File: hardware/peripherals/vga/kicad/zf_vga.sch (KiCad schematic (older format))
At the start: 35 parts

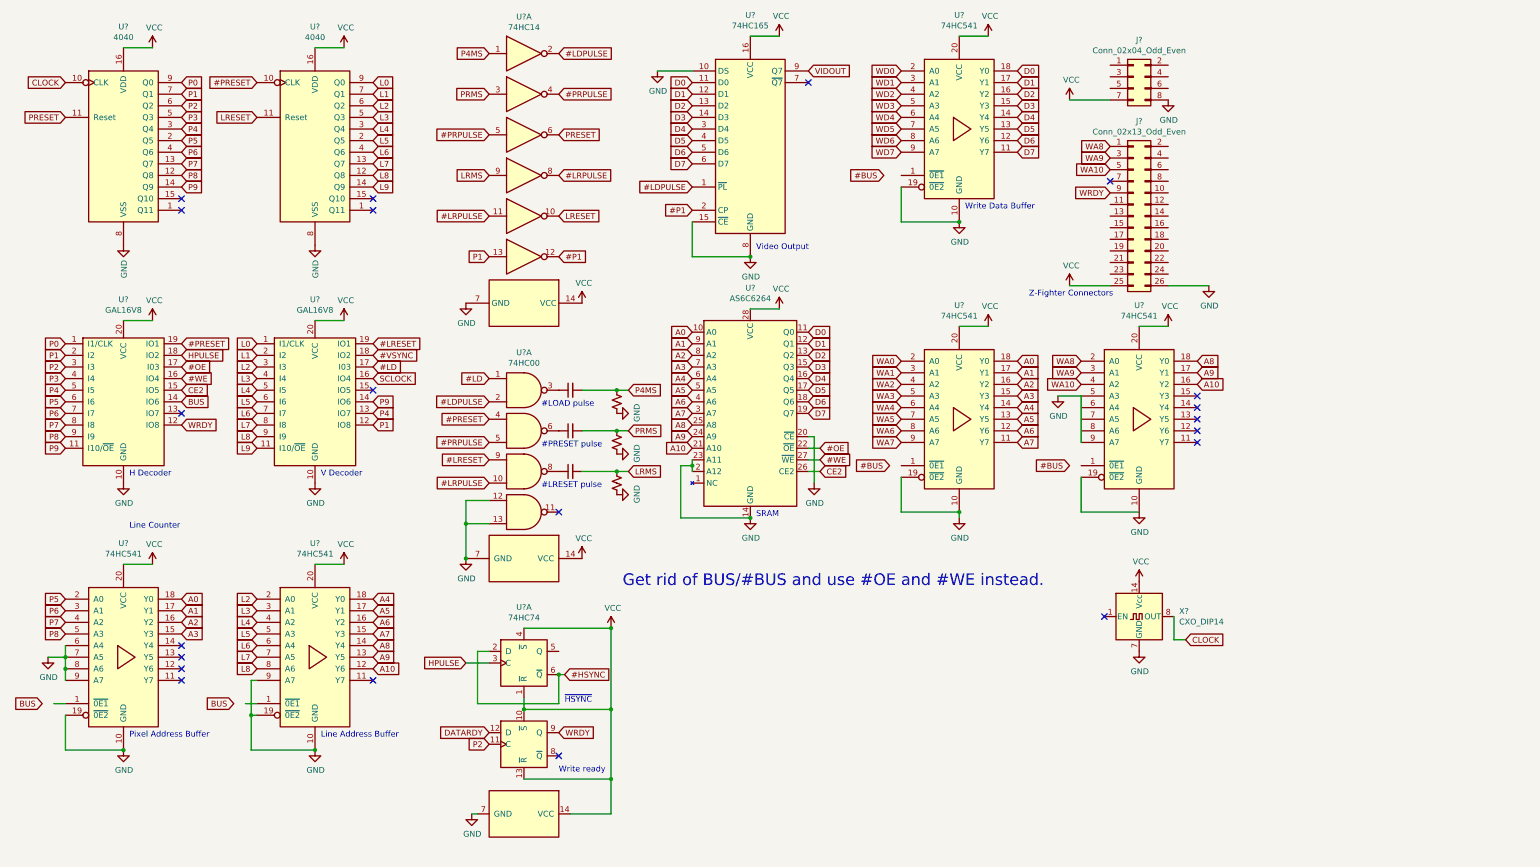
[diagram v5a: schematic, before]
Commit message: Changed /hsync to set/reset on flip flop, changed bus to /we and /oe
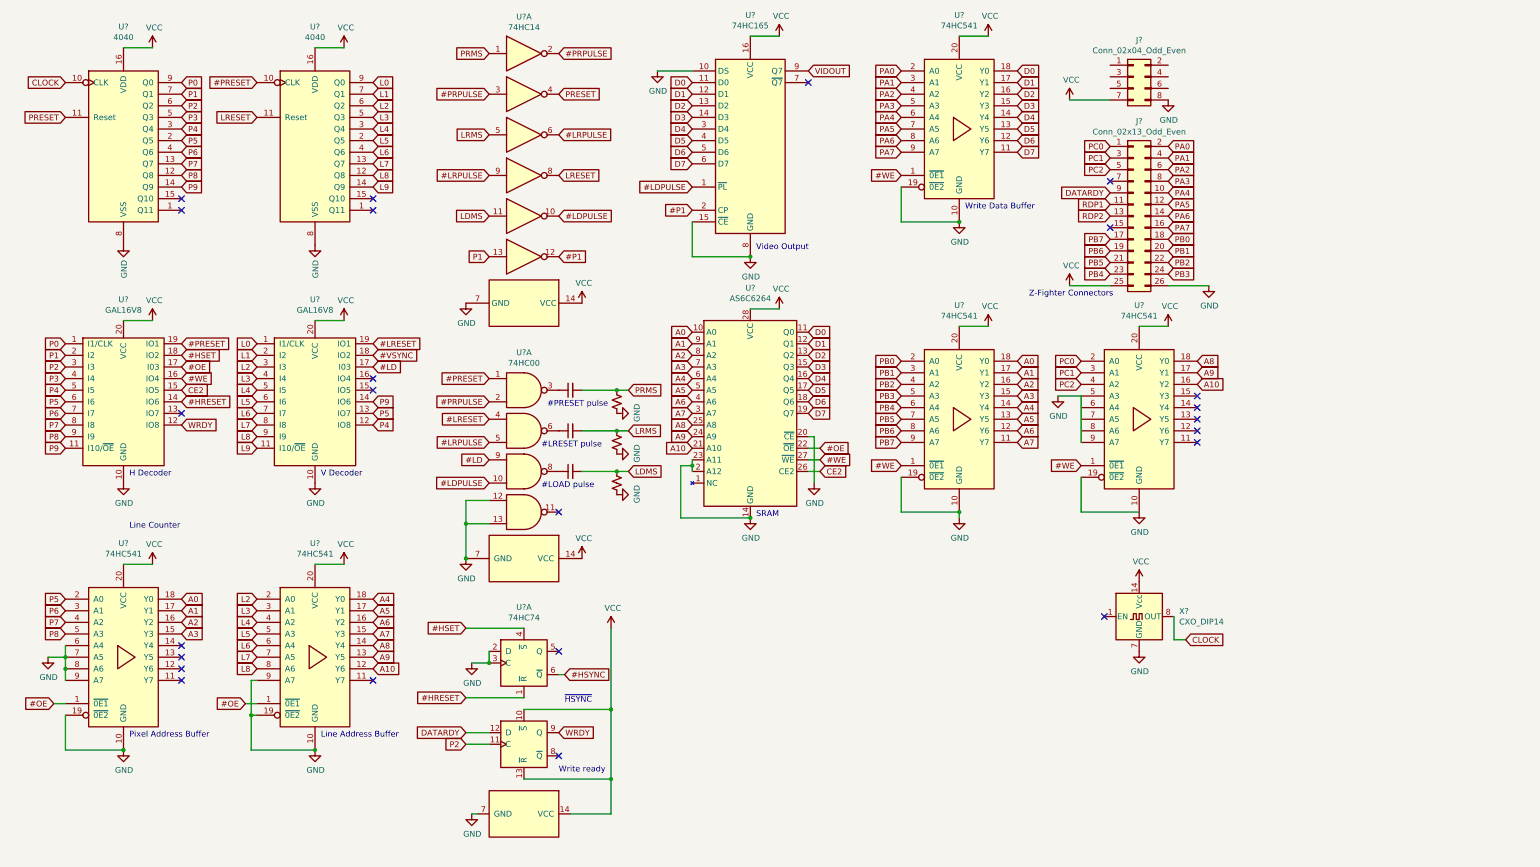
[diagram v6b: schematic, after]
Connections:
- net WA0 is gone; now on net PB0: U?.2 (A0)
- net WA1 is gone; now on net PB1: U?.3 (A1)
- net WA2 is gone; now on net PB2: U?.4 (A2)
- net WA3 is gone; now on net PB3: U?.5 (A3)
- net WA4 is gone; now on net PB4: U?.6 (A4)
- net WA5 is gone; now on net PB5: U?.7 (A5)
- net WA6 is gone; now on net PB6: U?.8 (A6)
- net WA7 is gone; now on net PB7: U?.9 (A7)
- net WD0 is gone; now on net PA0: U?.2 (A0)
- net WD1 is gone; now on net PA1: U?.3 (A1)
- net WD2 is gone; now on net PA2: U?.4 (A2)
- net WD3 is gone; now on net PA3: U?.5 (A3)
- net WD4 is gone; now on net PA4: U?.6 (A4)
- net WD5 is gone; now on net PA5: U?.7 (A5)
- net WD6 is gone; now on net PA6: U?.8 (A6)
- net WD7 is gone; now on net PA7: U?.9 (A7)
- net #HSYNC: no longer U?.2 (D)
- net #LD: now also U?.9; no longer U?.1
- net #LDPULSE: now also U?.10, U?.10; no longer U?.2, U?.2
- net #LRESET: now also U?.4; no longer U?.9
- net #LRPULSE: now also U?.5, U?.6, U?.9; no longer U?.10, U?.11, U?.8
- net #OE: now also U?.1 (~0E1), U?.1 (~0E1)
- net #PRESET: now also U?.1; no longer U?.4
- net #PRPULSE: now also U?.2, U?.2, U?.3; no longer U?.4, U?.5, U?.5
- net #WE: now also U?.1 (~0E1), U?.1 (~0E1), U?.1 (~0E1)
- net DATARDY: now also J?.9 (Pin_9)
- net GND: now also U?.2 (D), U?.3 (C)
- net LRESET: now also U?.8; no longer U?.10
- net LRMS: now also U?.5; no longer U?.9
- net P1: no longer U?.12 (IO8)
- net P4: now also U?.12 (IO8); no longer U?.13 (IO7)
- net P5: now also U?.13 (IO7)
- net PRESET: now also U?.4; no longer U?.6
- net PRMS: now also U?.1; no longer U?.3
- net VCC: no longer U?.1 (~R), U?.4 (~S)
- net WRDY: no longer J?.9 (Pin_9)
- net PA4: now reaches J?.10 (Pin_10)
- net RDP1: now reaches J?.11 (Pin_11)
- net PA5: now reaches J?.12 (Pin_12)
- net RDP2: now reaches J?.13 (Pin_13)
- net PA6: now reaches J?.14 (Pin_14)
- net PA7: now reaches J?.16 (Pin_16)
- net PB7: now reaches J?.17 (Pin_17)
- net PB0: now reaches J?.18 (Pin_18)
- net PB6: now reaches J?.19 (Pin_19)
- net PA0: now reaches J?.2 (Pin_2)
- net PB1: now reaches J?.20 (Pin_20)
- net PB5: now reaches J?.21 (Pin_21)
- net PB2: now reaches J?.22 (Pin_22)
- net PB4: now reaches J?.23 (Pin_23)
- net PB3: now reaches J?.24 (Pin_24)
- net PA1: now reaches J?.4 (Pin_4)
- net PA2: now reaches J?.6 (Pin_6)
- net PA3: now reaches J?.8 (Pin_8)
- net at U?.3: now also C?.1; no longer C?.1
- net at U?.6: now also C?.1; no longer C?.1
- net at U?.8: now also C?.1; no longer C?.1
- net BUS renamed #HRESET
- net #HRESET: now also U?.1 (~R)
- net HPULSE renamed #HSET
- net #HSET: now also U?.4 (~S); no longer U?.3 (C)
- net P4MS renamed LDMS
- net LDMS: now also U?.11; no longer U?.1
- net SCLOCK: no longer names the net of U?.16 (IO4)
- net WA10 renamed PC2
- net WA8 renamed PC0
- net WA9 renamed PC1
- no-connect marks 21 -> 24
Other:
- note removed: "Get rid of BUS/#BUS and use #OE and #WE instead."

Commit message: Controller, VGA ports, adjusted write timings
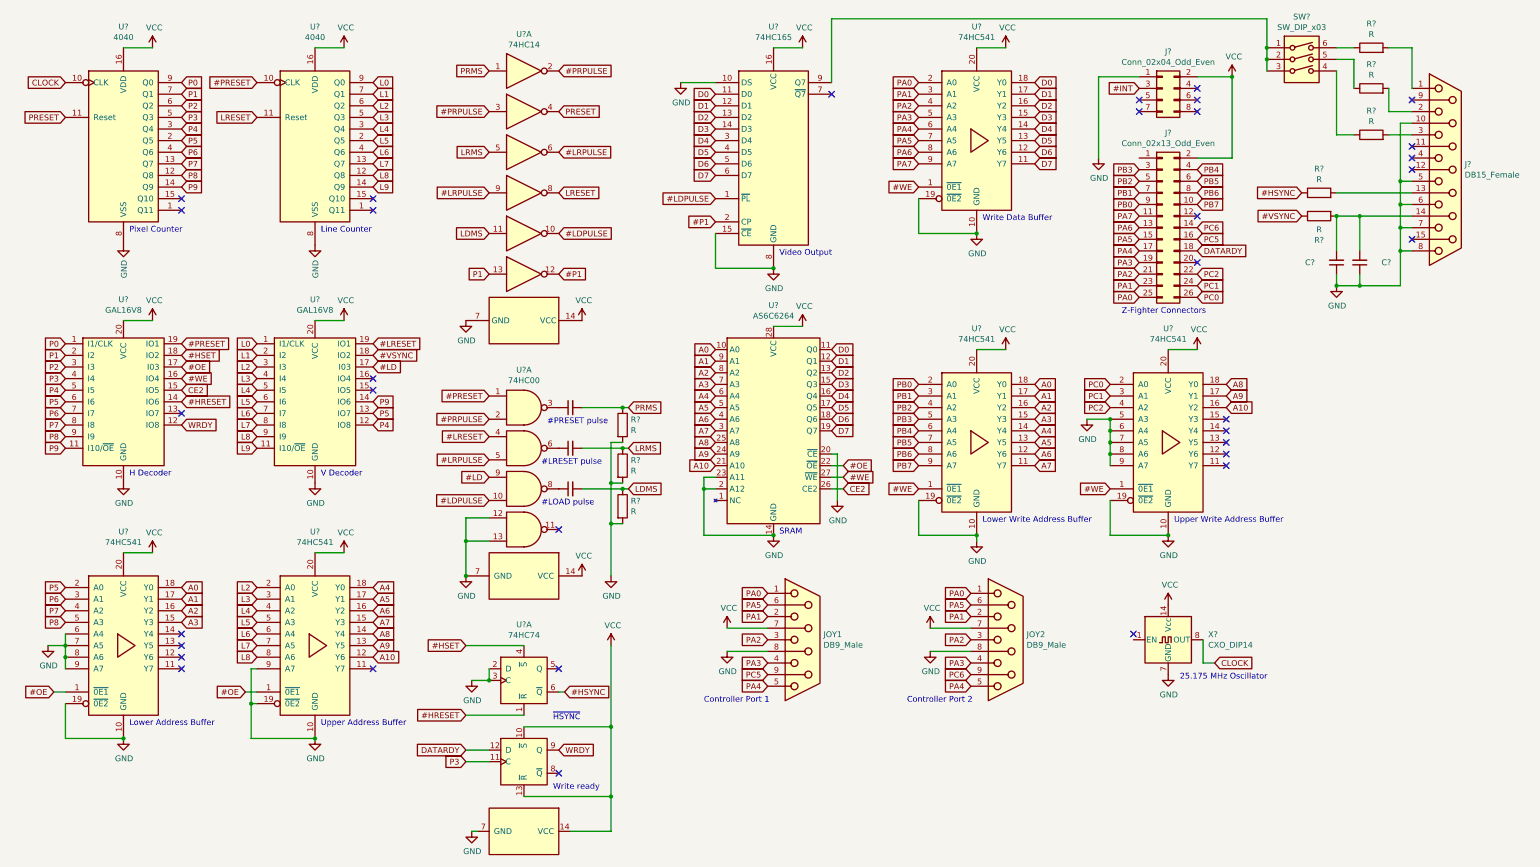
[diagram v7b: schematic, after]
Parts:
- removed R? (x3): R_Small_US, symbol Device:R_Small_US
- added C? (x2): C_Small, symbol Device:C_Small
- added J?: DB15_Female, symbol Connector:DB15_Female
- added JOY1, JOY2: DB9_Male, Connector_Dsub:DSUB-9_Male_Horizontal_P2.77x2.84mm_EdgePinOffset7.70mm_Housed_MountingHolesOffset9.12mm, symbol Connector:DB9_Female
- added R? (x8): R, symbol Device:R
- added SW?: SW_DIP_x03, symbol Switch:SW_DIP_x03
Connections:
- net RDP1 is gone; now on net PA7: J?.11 (Pin_11)
- net RDP2 is gone; now on net PA6: J?.13 (Pin_13)
- net #HSYNC: now also R?.1
- net #VSYNC: now also R?.1
- net DATARDY: now also J?.18 (Pin_18); no longer J?.9 (Pin_9)
- net GND: now also J?.1 (Pin_1), U?.6 (A4), U?.7 (A5), U?.8 (A6), C?.1, C?.1, J?.10 (P10), J?.5, J?.6, J?.7, J?.8, JOY1.8, JOY2.8, R?.2, R?.2, R?.2; no longer J?.26 (Pin_26), J?.8 (Pin_8)
- net LDMS: now also R?.1
- net LRMS: now also R?.1
- net P2: no longer U?.11 (C)
- net P3: now also U?.11 (C)
- net PA0: now also J?.25 (Pin_25), JOY1.1, JOY2.1; no longer J?.2 (Pin_2)
- net PA1: now also J?.23 (Pin_23), JOY1.2, JOY2.2; no longer J?.4 (Pin_4)
- net PA2: now also J?.21 (Pin_21), JOY1.3, JOY2.3; no longer J?.6 (Pin_6)
- net PA3: now also J?.19 (Pin_19), JOY1.4, JOY2.4; no longer J?.8 (Pin_8)
- net PA4: now also J?.17 (Pin_17), JOY1.5, JOY2.5; no longer J?.10 (Pin_10)
- net PA5: now also J?.15 (Pin_15), JOY1.6, JOY2.6; no longer J?.12 (Pin_12)
- net PA6: no longer J?.14 (Pin_14)
- net PA7: no longer J?.16 (Pin_16)
- net PB0: now also J?.9 (Pin_9); no longer J?.18 (Pin_18)
- net PB1: now also J?.7 (Pin_7); no longer J?.20 (Pin_20)
- net PB2: now also J?.5 (Pin_5); no longer J?.22 (Pin_22)
- net PB3: now also J?.3 (Pin_3); no longer J?.24 (Pin_24)
- net PB4: now also J?.4 (Pin_4); no longer J?.23 (Pin_23)
- net PB5: now also J?.6 (Pin_6); no longer J?.21 (Pin_21)
- net PB6: now also J?.8 (Pin_8); no longer J?.19 (Pin_19)
- net PB7: now also J?.10 (Pin_10); no longer J?.17 (Pin_17)
- net PC0: now also J?.26 (Pin_26); no longer J?.1 (Pin_1)
- net PC1: now also J?.24 (Pin_24); no longer J?.3 (Pin_3)
- net PC2: now also J?.22 (Pin_22); no longer J?.5 (Pin_5)
- net PRMS: now also R?.1
- net VCC: now also J?.2 (Pin_2), J?.2 (Pin_2), JOY1.7, JOY2.7; no longer J?.25 (Pin_25), J?.7 (Pin_7)
- net #INT: now reaches J?.3 (Pin_3)
- net VIDOUT: no longer names the net of U?.9 (Q7)
- net VIDOUT: now also SW?.1, SW?.2, SW?.3
- new net: J?.1, R?.2
- new net: J?.13 (P13), R?.2
- new net: C?.2, C?.2, J?.14 (P14), R?.2
- new net: J?.2, R?.2
- new net: J?.3, R?.2
- new net: R?.1, SW?.4
- new net: R?.1, SW?.5
- new net: R?.1, SW?.6
- new net PC5: J?.16 (Pin_16), JOY1.9
- new net PC6: J?.14 (Pin_14), JOY2.9
- no-connect marks 24 -> 34
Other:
- note added: "25.175 MHz Oscillator"
- note added: "Controller Port 1"
- note added: "Controller Port 2"
- note added: "Lower Address Buffer"
- note added: "Lower Write Address Buffer"
- note added: "Pixel Counter"
- note added: "Upper Address Buffer"
- note added: "Upper Write Address Buffer"
- note removed: "Line Address Buffer"
- note removed: "Pixel Address Buffer"
- moved on the sheet: J?, U?, U?A, X?

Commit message: Footprints
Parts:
- J3: renamed from J?; footprint (none) -> Connector_Dsub:DSUB-15-HD_Female_Horizontal_P2.29x1.98mm_EdgePinOffset8.35mm_Housed_MountingHolesOffset10.89mm
- U1, U10, U2: renamed from U?; footprint (none) -> Package_DIP:DIP-16_W7.62mm
- U12, U13, U14, U3, U4, U5, U6: renamed from U?; footprint (none) -> Package_DIP:DIP-20_W7.62mm
- U7, U9: renamed from U?; footprint (none) -> Package_DIP:DIP-14_W7.62mm
- U8: renamed from U?; value 74HC14 -> 74HC04; footprint (none) -> Package_DIP:DIP-14_W7.62mm
- gave numbers to parts that had none: 19
- renumbered JOY1 to J4, JOY2 to J5
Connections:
- net GND: now also J2.1 (Pin_1)
- net P3: no longer U9.11 (C)
- net P4: now also U9.11 (C)
- net #INT: no longer names the net of J1.3 (Pin_3)
- no-connect marks 34 -> 35
